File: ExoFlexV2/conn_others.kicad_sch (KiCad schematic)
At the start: 10 parts

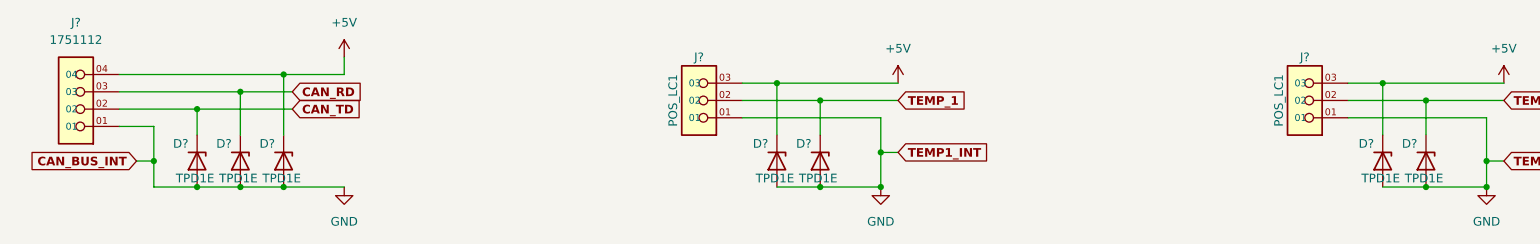
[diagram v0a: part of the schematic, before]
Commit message: Mise à jour signaux STM
- Condo de découplage
- Signaux supplémentaire pour le STM
- Page GND sera pour Multiplexeur
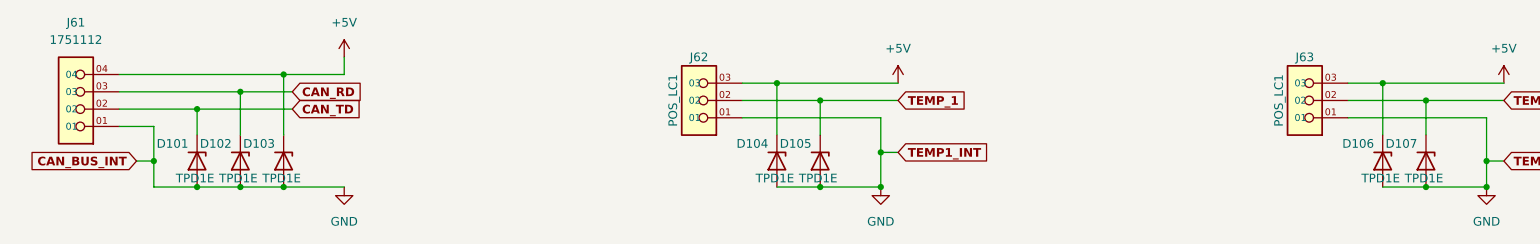
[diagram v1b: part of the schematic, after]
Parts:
- gave numbers to parts that had none: 10
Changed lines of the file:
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@@
   (symbol (lib_id "Device:D_Zener") (at 60.96 95.25 270) (unit 1)
     (in_bom yes) (on_board yes)
-    (property "Reference" "D?" (id 0) (at 59.69 92.71 90)
+    (property "Reference" "D102" (id 0) (at 59.69 92.71 90)
       (effects (font (size 1.27 1.27)) (justify right))
     )
@@
   (symbol (lib_id "power:GND") (at 154.94 99.06 0) (unit 1)
     (in_bom yes) (on_board yes) (fields_autoplaced)
-    (property "Reference" "#PWR?" (id 0) (at 154.94 105.41 0)
+    (property "Reference" "#PWR0119" (id 0) (at 154.94 105.41 0)
       (effects (font (size 1.27 1.27)) hide)
     )
@@
   (symbol (lib_id "SymLib:1751112") (at 33.02 85.09 180) (unit 1)
     (in_bom yes) (on_board yes)
-    (property "Reference" "J?" (id 0) (at 36.83 74.93 0))
+    (property "Reference" "J61" (id 0) (at 36.83 74.93 0))
     (property "Value" "1751112" (id 1) (at 36.83 77.47 0))
     (property "Footprint" "FootPrint:PHOENIX_1751112" (id 2) (at 33.02 85.09 0)
@@
   (symbol (lib_id "Device:D_Zener") (at 54.61 95.25 270) (unit 1)
     (in_bom yes) (on_board yes)
-    (property "Reference" "D?" (id 0) (at 53.34 92.71 90)
+    (property "Reference" "D101" (id 0) (at 53.34 92.71 90)
       (effects (font (size 1.27 1.27)) (justify right))
     )
@@
   (symbol (lib_id "power:GND") (at 243.84 99.06 0) (unit 1)
     (in_bom yes) (on_board yes) (fields_autoplaced)
-    (property "Reference" "#PWR?" (id 0) (at 243.84 105.41 0)
+    (property "Reference" "#PWR0121" (id 0) (at 243.84 105.41 0)
       (effects (font (size 1.27 1.27)) hide)
     )
@@
   (symbol (lib_id "power:+5V") (at 246.38 83.82 0) (unit 1)
     (in_bom yes) (on_board yes) (fields_autoplaced)
-    (property "Reference" "#PWR?" (id 0) (at 246.38 87.63 0)
+    (property "Reference" "#PWR0122" (id 0) (at 246.38 87.63 0)
       (effects (font (size 1.27 1.27)) hide)
     )
@@
   (symbol (lib_id "SymLib:1751109") (at 124.46 86.36 180) (unit 1)
     (in_bom yes) (on_board yes)
-    (property "Reference" "J?" (id 0) (at 128.27 80.01 0))
+    (property "Reference" "J62" (id 0) (at 128.27 80.01 0))
     (property "Value" "POS_LC1" (id 1) (at 124.46 86.36 90))
     (property "Footprint" "FootPrint:PHOENIX_1751109" (id 2) (at 124.46 86.36 0)
@@
   (symbol (lib_id "Device:D_Zener") (at 67.31 95.25 270) (unit 1)
     (in_bom yes) (on_board yes)
-    (property "Reference" "D?" (id 0) (at 66.04 92.71 90)
+    (property "Reference" "D103" (id 0) (at 66.04 92.71 90)
       (effects (font (size 1.27 1.27)) (justify right))
     )
@@
   (symbol (lib_id "power:+5V") (at 157.48 83.82 0) (unit 1)
     (in_bom yes) (on_board yes) (fields_autoplaced)
-    (property "Reference" "#PWR?" (id 0) (at 157.48 87.63 0)
+    (property "Reference" "#PWR0120" (id 0) (at 157.48 87.63 0)
       (effects (font (size 1.27 1.27)) hide)
     )
@@
   (symbol (lib_id "Device:D_Zener") (at 234.95 95.25 270) (unit 1)
     (in_bom yes) (on_board yes)
-    (property "Reference" "D?" (id 0) (at 233.68 92.71 90)
+    (property "Reference" "D107" (id 0) (at 233.68 92.71 90)
       (effects (font (size 1.27 1.27)) (justify right))
     )
@@
   (symbol (lib_id "Device:D_Zener") (at 228.6 95.25 270) (unit 1)
     (in_bom yes) (on_board yes)
-    (property "Reference" "D?" (id 0) (at 227.33 92.71 90)
+    (property "Reference" "D106" (id 0) (at 227.33 92.71 90)
       (effects (font (size 1.27 1.27)) (justify right))
     )
@@
   (symbol (lib_id "SymLib:1751109") (at 213.36 86.36 180) (unit 1)
     (in_bom yes) (on_board yes)
-    (property "Reference" "J?" (id 0) (at 217.17 80.01 0))
+    (property "Reference" "J63" (id 0) (at 217.17 80.01 0))
     (property "Value" "POS_LC1" (id 1) (at 213.36 86.36 90))
     (property "Footprint" "FootPrint:PHOENIX_1751109" (id 2) (at 213.36 86.36 0)
@@
   (symbol (lib_id "Device:D_Zener") (at 146.05 95.25 270) (unit 1)
     (in_bom yes) (on_board yes)
-    (property "Reference" "D?" (id 0) (at 144.78 92.71 90)
+    (property "Reference" "D105" (id 0) (at 144.78 92.71 90)
       (effects (font (size 1.27 1.27)) (justify right))
     )
@@
   (symbol (lib_id "Device:D_Zener") (at 139.7 95.25 270) (unit 1)
     (in_bom yes) (on_board yes)
-    (property "Reference" "D?" (id 0) (at 138.43 92.71 90)
+    (property "Reference" "D104" (id 0) (at 138.43 92.71 90)
       (effects (font (size 1.27 1.27)) (justify right))
     )
@@
   (symbol (lib_id "power:+5V") (at 76.2 80.01 0) (unit 1)
     (in_bom yes) (on_board yes) (fields_autoplaced)
-    (property "Reference" "#PWR?" (id 0) (at 76.2 83.82 0)
+    (property "Reference" "#PWR0117" (id 0) (at 76.2 83.82 0)
       (effects (font (size 1.27 1.27)) hide)
     )
@@
   (symbol (lib_id "power:GND") (at 76.2 99.06 0) (unit 1)
     (in_bom yes) (on_board yes) (fields_autoplaced)
-    (property "Reference" "#PWR?" (id 0) (at 76.2 105.41 0)
-      (effects (font (size 1.27 1.27)) hide)
-    )
+    (property "Reference" "#PWR0118" (id 0) (at 76.2 105.41 0)
+      (effects (font (size 1.27 1.27)) hide)
+    )

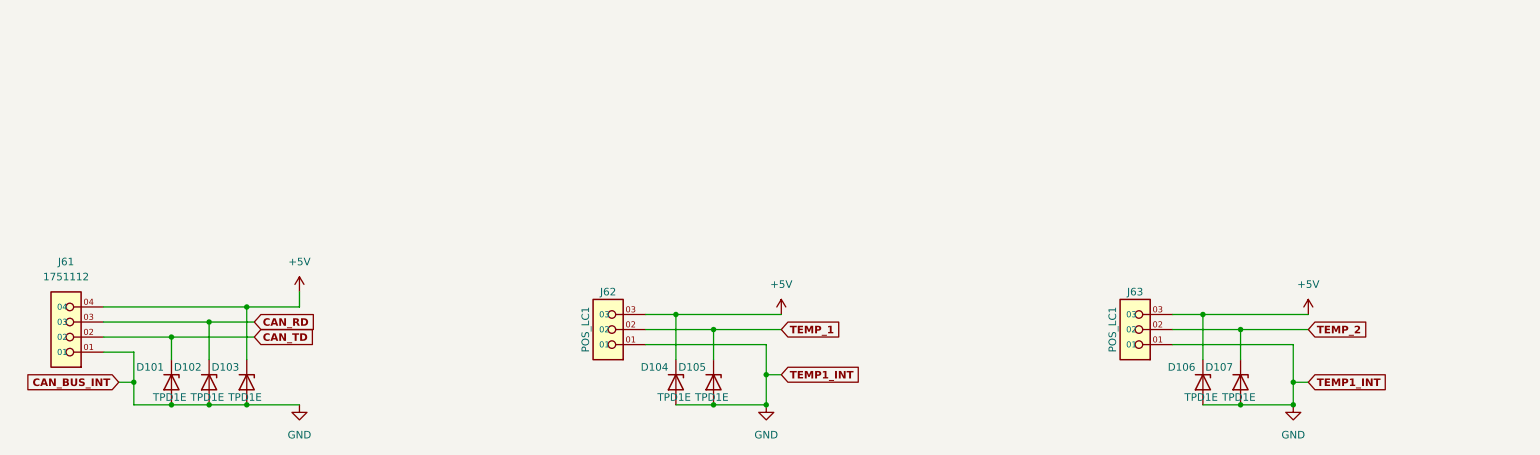
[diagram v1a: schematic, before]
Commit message: Finalisation 1
- Ajout de pages pour la gestion des signaux négatif
- Modification des pages de torque et amplitude
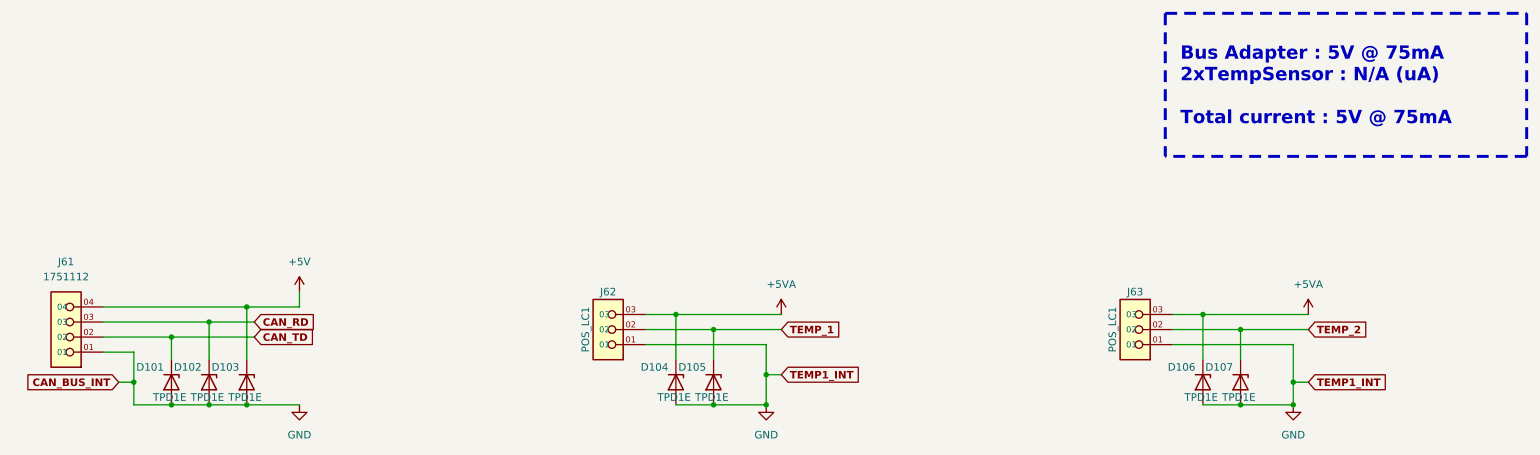
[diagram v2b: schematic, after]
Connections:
- net +5V: no longer D104.1 (K), D106.1 (K), J62.03, J63.03
- new net +5VA: D104.1 (K), D106.1 (K), J62.03, J63.03
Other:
- note added: "Bus Adapter : 5V @ 75mA 2xTempSensor : N/A (uA) Total current : 5V @ 75mA"
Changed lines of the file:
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@@
     (stroke (width 0) (type default) (color 0 0 0 0))
+  )
+  (polyline (pts (xy 283.21 33.02) (xy 283.21 57.15))
+    (stroke (width 0.5) (type dash) (color 255 148 44 1))
   )
   (wire (pts (xy 243.84 95.25) (xy 243.84 99.06))
     (stroke (width 0) (type default) (color 0 0 0 0))
   )
+  (polyline (pts (xy 222.25 33.02) (xy 222.25 57.15))
+    (stroke (width 0.5) (type dash) (color 255 148 44 1))
+  )
   (wire (pts (xy 54.61 87.63) (xy 54.61 91.44))
     (stroke (width 0) (type default) (color 0 0 0 0))
@@
     (stroke (width 0) (type default) (color 0 0 0 0))
   )
+  (polyline (pts (xy 283.21 57.15) (xy 222.25 57.15))
+    (stroke (width 0.5) (type dash) (color 255 148 44 1))
+  )
   (wire (pts (xy 234.95 99.06) (xy 243.84 99.06))
     (stroke (width 0) (type default) (color 0 0 0 0))
@@
     (stroke (width 0) (type default) (color 0 0 0 0))
   )
+  (polyline (pts (xy 222.25 33.02) (xy 283.21 33.02))
+    (stroke (width 0.5) (type dash) (color 255 148 44 1))
+  )
   (wire (pts (xy 134.62 83.82) (xy 139.7 83.82))
     (stroke (width 0) (type default) (color 0 0 0 0))
@@
   (wire (pts (xy 43.18 87.63) (xy 54.61 87.63))
     (stroke (width 0) (type default) (color 0 0 0 0))
+  )
+  (text "Bus Adapter : 5V @ 75mA\n2xTempSensor : N/A (uA)\n\nTotal current : 5V @ 75mA"
+    (at 224.79 52.07 0)
+    (effects (font (size 2.25 2.25) (thickness 0.5) bold) (justify left bottom))
   )
   (global_label "TEMP_2" (shape input) (at 246.38 86.36 0) (fields_autoplaced)
@@
     (pin "1")
   )
+  (symbol (lib_id "power:+5VA") (at 246.38 83.82 0) (unit 1)
+    (in_bom yes) (on_board yes) (fields_autoplaced)
+    (property "Reference" "#PWR?" (id 0) (at 246.38 87.63 0)
+      (effects (font (size 1.27 1.27)) hide)
+    )
+    (property "Value" "+5VA" (id 1) (at 246.38 78.74 0))
+    (property "Footprint" "" (id 2) (at 246.38 83.82 0)
+      (effects (font (size 1.27 1.27)) hide)
+    )
+    (property "Datasheet" "" (id 3) (at 246.38 83.82 0)
+      (effects (font (size 1.27 1.27)) hide)
+    )
+    (pin "1")
+  )
   (symbol (lib_id "SymLib:1751112") (at 33.02 85.09 180) (unit 1)
     (in_bom yes) (on_board yes)
@@
     (pin "1")
   )
-  (symbol (lib_id "power:+5V") (at 246.38 83.82 0) (unit 1)
-    (in_bom yes) (on_board yes) (fields_autoplaced)
-    (property "Reference" "#PWR0122" (id 0) (at 246.38 87.63 0)
-      (effects (font (size 1.27 1.27)) hide)
-    )
-    (property "Value" "+5V" (id 1) (at 246.38 78.74 0))
-    (property "Footprint" "" (id 2) (at 246.38 83.82 0)
-      (effects (font (size 1.27 1.27)) hide)
-    )
-    (property "Datasheet" "" (id 3) (at 246.38 83.82 0)
-      (effects (font (size 1.27 1.27)) hide)
-    )
-    (pin "1")
-  )
   (symbol (lib_id "SymLib:1751109") (at 124.46 86.36 180) (unit 1)
     (in_bom yes) (on_board yes)
@@
     (pin "2")
   )
-  (symbol (lib_id "power:+5V") (at 157.48 83.82 0) (unit 1)
-    (in_bom yes) (on_board yes) (fields_autoplaced)
-    (property "Reference" "#PWR0120" (id 0) (at 157.48 87.63 0)
-      (effects (font (size 1.27 1.27)) hide)
-    )
-    (property "Value" "+5V" (id 1) (at 157.48 78.74 0))
-    (property "Footprint" "" (id 2) (at 157.48 83.82 0)
-      (effects (font (size 1.27 1.27)) hide)
-    )
-    (property "Datasheet" "" (id 3) (at 157.48 83.82 0)
-      (effects (font (size 1.27 1.27)) hide)
-    )
-    (pin "1")
-  )
   (symbol (lib_id "Device:D_Zener") (at 234.95 95.25 270) (unit 1)
     (in_bom yes) (on_board yes)
@@
     (pin "2")
   )
+  (symbol (lib_id "power:+5VA") (at 157.48 83.82 0) (unit 1)
+    (in_bom yes) (on_board yes) (fields_autoplaced)
+    (property "Reference" "#PWR?" (id 0) (at 157.48 87.63 0)
+      (effects (font (size 1.27 1.27)) hide)
+    )
+    (property "Value" "+5VA" (id 1) (at 157.48 78.74 0))
+    (property "Footprint" "" (id 2) (at 157.48 83.82 0)
+      (effects (font (size 1.27 1.27)) hide)
+    )
+    (property "Datasheet" "" (id 3) (at 157.48 83.82 0)
+      (effects (font (size 1.27 1.27)) hide)
+    )
+    (pin "1")
+  )
   (symbol (lib_id "power:+5V") (at 76.2 80.01 0) (unit 1)
